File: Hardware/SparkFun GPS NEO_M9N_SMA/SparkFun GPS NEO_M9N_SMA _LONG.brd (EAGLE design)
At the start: 40.6 x 36.8 mm, 93 parts, among them J2 Qwiic Right Angle, J4 Qwiic Right Angle, U1 U-BLOX_NEO-M9N, U2 3.3V

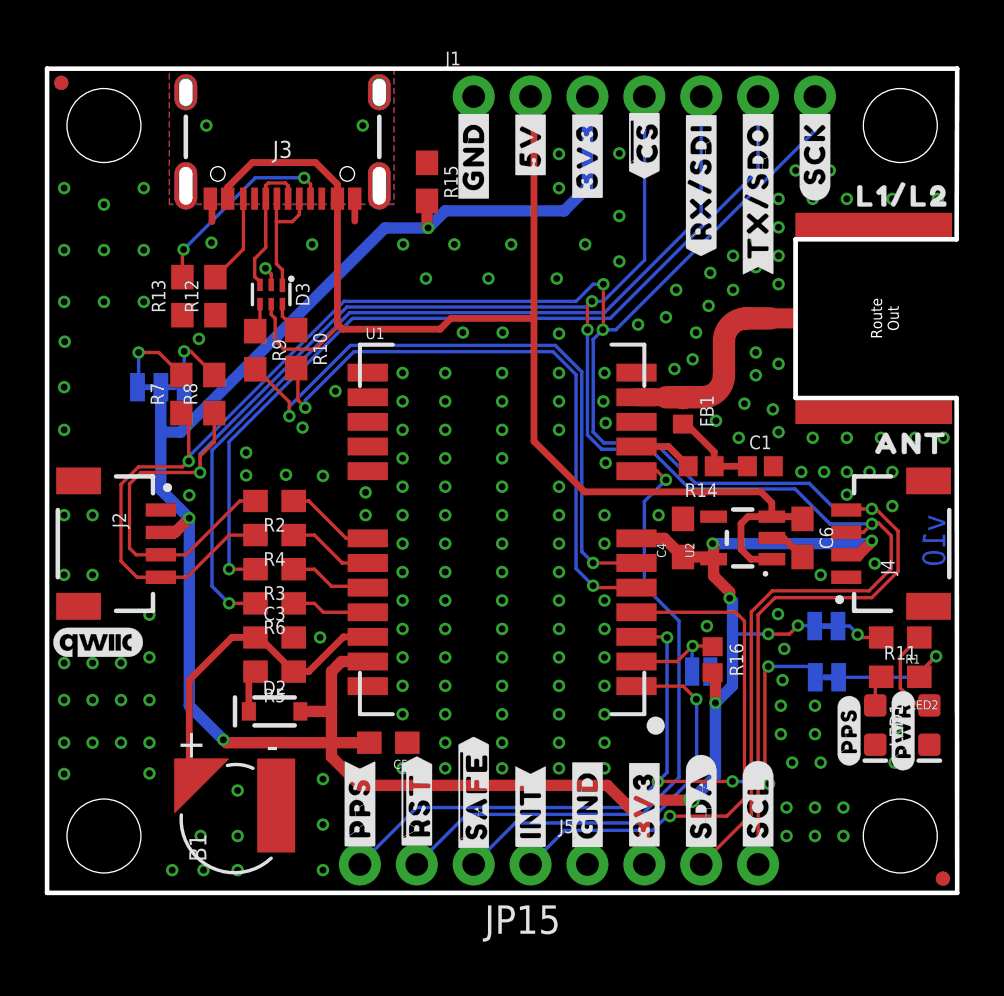
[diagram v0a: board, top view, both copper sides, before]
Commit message: Updates SMD, SMA connector with new footprint
* Fixes connector label in schematic
* Fixes LED labels
* Fixes TX/SDO label
* Adds VCC Range to regulator
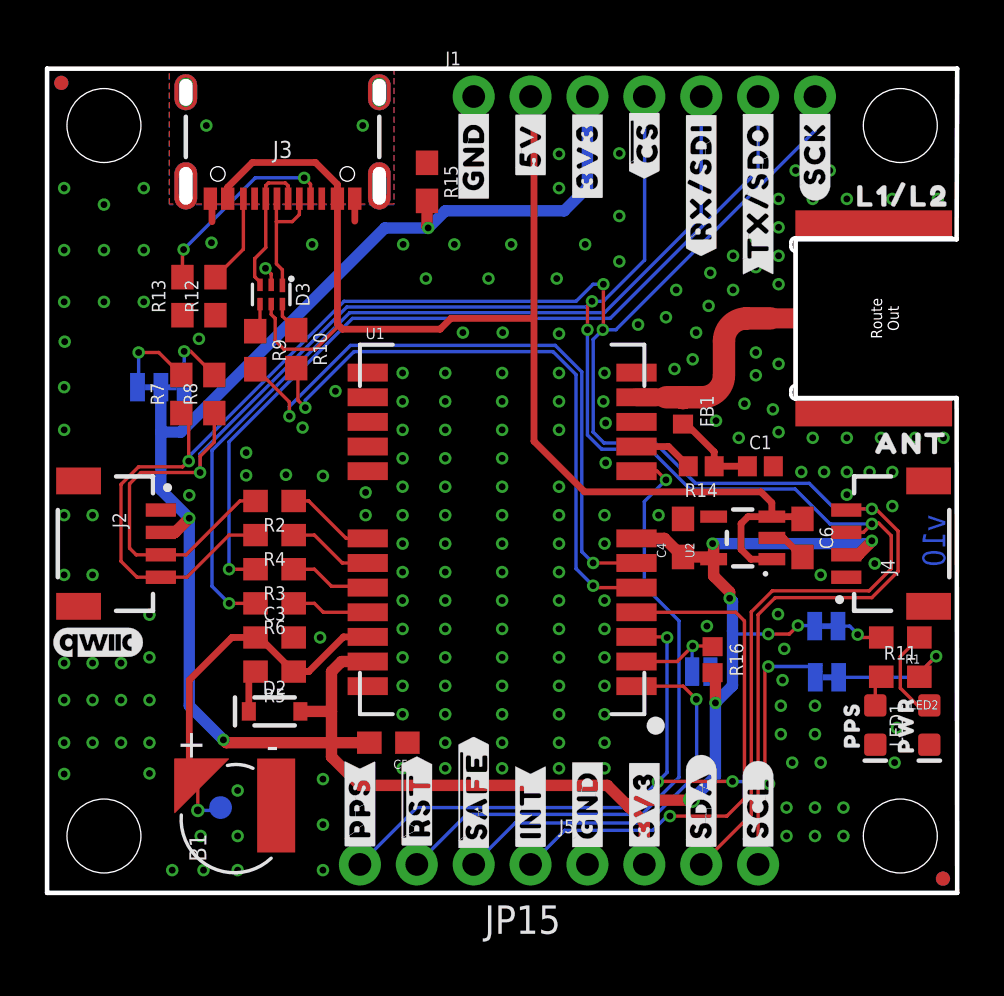
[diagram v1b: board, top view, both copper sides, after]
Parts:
- added TP1: TEST-POINT3X4, SparkFun-Connectors:PAD.03X.04
- U$10: device gps:#PPS#7 -> gps:PPS7
- U$13: device gps:#PWR#6 -> gps:PWR6
- U$37: device gps2:#TX#SDI#5 -> gps2:#TX#SDO#5
- moved U$37 0.38 mm to (31.8, 31.4)
- moved U$10 0.28 mm to (35.9, 7.49)
- moved U$13 0.28 mm to (38.4, 7.49)
- moved U$29 0.13 mm to (5.08, 24.3)
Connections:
- net RXI/SDO renamed RXI/SDI
- net TXO/SDI renamed TXO/SDO
- net V_BATT: now also TP1.P$1
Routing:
- net V_BATT: track 14.2 -> 17.1 mm, vias 0 -> 1
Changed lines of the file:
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@@
 <layer number="27" name="tValues" color="7" fill="1" visible="no" active="yes"/>
 <layer number="28" name="bValues" color="7" fill="1" visible="no" active="yes"/>
-<layer number="29" name="tStop" color="7" fill="3" visible="no" active="yes"/>
+<layer number="29" name="tStop" color="7" fill="3" visible="yes" active="yes"/>
 <layer number="30" name="bStop" color="7" fill="6" visible="no" active="yes"/>
-<layer number="31" name="tCream" color="7" fill="4" visible="no" active="yes"/>
+<layer number="31" name="tCream" color="7" fill="4" visible="yes" active="yes"/>
 <layer number="32" name="bCream" color="7" fill="5" visible="no" active="yes"/>
 <layer number="33" name="tFinish" color="6" fill="3" visible="no" active="yes"/>
@@
 <layer number="44" name="Drills" color="7" fill="1" visible="no" active="yes"/>
 <layer number="45" name="Holes" color="7" fill="1" visible="yes" active="yes"/>
-<layer number="46" name="Milling" color="3" fill="1" visible="no" active="yes"/>
+<layer number="46" name="Milling" color="3" fill="1" visible="yes" active="yes"/>
 <layer number="47" name="Measures" color="7" fill="1" visible="no" active="yes"/>
 <layer number="48" name="Document" color="7" fill="1" visible="no" active="yes"/>
@@
 <layer number="115" name="ReferenceISLANDS" color="7" fill="1" visible="no" active="no"/>
 <layer number="116" name="Patch_BOT" color="9" fill="4" visible="no" active="no"/>
-<layer number="117" name="PM_Ref" color="26" fill="1" visible="no" active="yes"/>
+<layer number="117" name="PM_Ref" color="26" fill="1" visible="yes" active="yes"/>
 <layer number="118" name="Rect_Pads" color="7" fill="1" visible="no" active="no"/>
-<layer number="119" name="PF_Ref" color="31" fill="1" visible="no" active="yes"/>
-<layer number="120" name="WFL_Ref" color="25" fill="1" visible="no" active="yes"/>
+<layer number="119" name="PF_Ref" color="31" fill="1" visible="yes" active="yes"/>
+<layer number="120" name="WFL_Ref" color="25" fill="1" visible="yes" active="yes"/>
 <layer number="121" name="_tsilk" color="7" fill="1" visible="no" active="no"/>
 <layer number="122" name="_bsilk" color="7" fill="1" visible="no" active="no"/>
@@
 <element name="U$8" library="gps" package="#GND#0" value="" x="19.05" y="32.893" smashed="yes" rot="R90"/>
 <element name="U$9" library="gps" package="#INT#16" value="" x="21.59" y="3.683" smashed="yes" rot="R90"/>
-<element name="U$10" library="gps" package="#PPS#7" value="" x="35.814" y="7.239" smashed="yes" rot="R90"/>
 <element name="U$11" library="gps" package="#PPS#13" value="" x="13.97" y="3.81" smashed="yes" rot="R90"/>
-<element name="U$13" library="gps" package="#PWR#6" value="" x="38.227" y="7.239" smashed="yes" rot="R90"/>
 <element name="U$15" library="gps" package="#RX#SDI#10" value="" x="29.21" y="31.75" smashed="yes" rot="R90"/>
 <element name="U$16" library="gps" package="#SCK#12" value="" x="34.29" y="33.02" smashed="yes" rot="R90"/>
@@
 <element name="U$28" library="gps2" package="##RST##2" value="" x="16.51" y="3.937" smashed="yes" rot="R90"/>
 <element name="U$22" library="gps2" package="##SAFE##11" value="" x="19.05" y="4.318" smashed="yes" rot="MR270"/>
-<element name="U$29" library="gps2" package="#I2C#3" value="" x="4.953" y="24.257" smashed="yes" rot="MR0"/>
+<element name="U$29" library="gps2" package="#I2C#3" value="" x="5.08" y="24.257" smashed="yes" rot="MR0"/>
 <element name="U$30" library="gps2" package="#INT#10" value="" x="21.59" y="3.683" smashed="yes" rot="MR270"/>
 <element name="U$31" library="gps2" package="#PPS#0" value="" x="37.719" y="9.652" smashed="yes" rot="MR0"/>
@@
 <element name="U$35" library="gps2" package="#SCL#8" value="" x="31.75" y="3.81" smashed="yes" rot="MR270"/>
 <element name="U$36" library="gps2" package="#SDA#9" value="" x="29.21" y="3.937" smashed="yes" rot="MR270"/>
-<element name="U$37" library="gps2" package="#TX#SDI#5" value="" x="31.75" y="31.75" smashed="yes" rot="MR270"/>
 <element name="U$38" library="gps" package="#GND#0" value="" x="19.05" y="32.893" smashed="yes" rot="MR270"/>
 <element name="U$39" library="gps" package="#3V3#6" value="" x="24.13" y="32.893" smashed="yes" rot="MR270"/>
@@
 <element name="U$41" library="gps" package="#GND#0" value="" x="24.13" y="3.937" smashed="yes" rot="MR270"/>
 <element name="U$42" library="gps" package="#5V#1" value="" x="21.59" y="33.401" smashed="yes" rot="MR270"/>
+<element name="TP1" library="SparkFun-Connectors" package="PAD.03X.04" value="TEST-POINT3X4" x="7.747" y="3.81" smashed="yes" rot="MR0"/>
+<element name="U$37" library="gps2" package="#TX#SDO#5" value="" x="31.75" y="31.369" smashed="yes" rot="MR270"/>
+<element name="U$10" library="gps" package="PPS7" value="" x="35.941" y="7.493" smashed="yes" rot="R90"/>
+<element name="U$13" library="gps" package="PWR6" value="" x="38.354" y="7.493" smashed="yes" rot="R90"/>
 </elements>
 <signals>
@@
 <wire x1="26.32" y1="9.2306" x2="28.4052875" y2="9.2306" width="0.1524" layer="1"/>
 </signal>
-<signal name="RXI/SDO">
+<signal name="RXI/SDI">
 <contactref element="R6" pad="2"/>
 <wire x1="9.31" y1="12.9286" x2="8.128" y2="12.9286" width="0.1524" layer="1"/>
@@
 <wire x1="24.892" y1="25.908" x2="29.21" y2="30.226" width="0.1524" layer="16"/>
 </signal>
-<signal name="TXO/SDI">
+<signal name="TXO/SDO">
 <contactref element="R3" pad="2"/>
 <wire x1="9.31" y1="14.4526" x2="8.128" y2="14.4526" width="0.1524" layer="1"/>
@@
 <wire x1="8.255" y1="11.4046" x2="6.35" y2="9.4996" width="0.3048" layer="1"/>
 <wire x1="13.234" y1="11.4306" x2="14.32" y2="11.4306" width="0.3048" layer="1"/>
+<contactref element="TP1" pad="P$1"/>
+<wire x1="6.35" y1="5.324" x2="6.731" y2="4.943" width="0.1524" layer="1"/>
+<wire x1="6.731" y1="4.943" x2="6.731" y2="3.683" width="0.1524" layer="1"/>
+<via x="6.731" y="3.683" extent="1-16" drill="0.35"/>
+<wire x1="6.731" y1="3.683" x2="7.62" y2="3.683" width="0.1524" layer="16"/>
+<wire x1="7.62" y1="3.683" x2="7.747" y2="3.81" width="0.1524" layer="16"/>
 </signal>
 </signals>
